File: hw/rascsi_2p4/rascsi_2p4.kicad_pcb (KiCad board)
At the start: 2 copper layers, 65 x 56 mm, 126 parts, among them J1 Raspberry_Pi_2_3, J10 Conn_01x04_Male, J2 DNP, J20 171826-4, J3 Conn_02x25_Odd_Even, J4 I2C Pinout, J5 DNP, J6 CONNFLY DB-25, J7 DNP, J8 USB_B_Micro, J9 Conn_02x25_Odd_Even, U1 74ALVC164245DGG, U2 74ALVC164245DGG, X1 Mac, X3 Mac, X7 Pi, X8 Pi

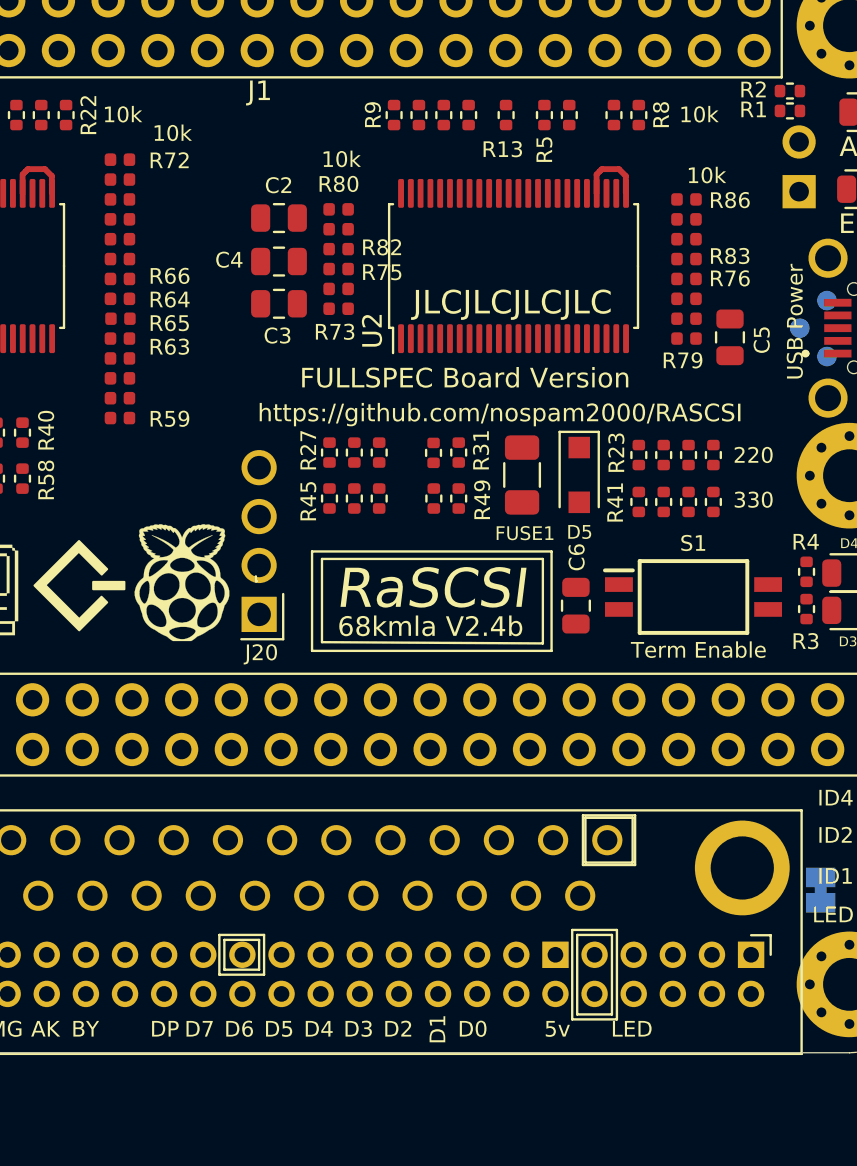
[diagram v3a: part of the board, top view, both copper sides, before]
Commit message: replaced R59-R86 by 100k to reduce power dissipation
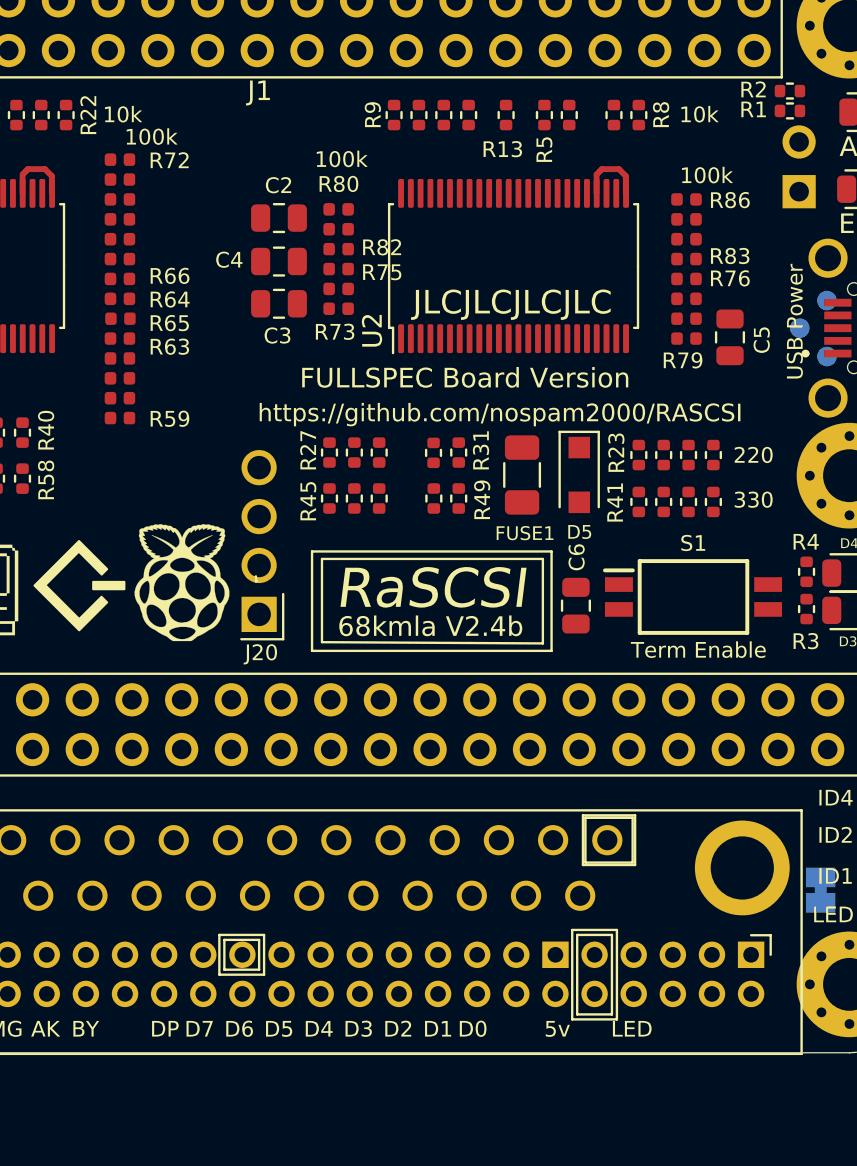
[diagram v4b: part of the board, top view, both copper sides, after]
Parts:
- R59, R60, R61, R62, R63, R64, R65, R66, R67, R68, R69, R70, R71, R72, R73, R74, R75, R76, R77, R78, R79, R80, R81, R82, R83, R84, R85, R86: value 10k -> 100k
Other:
- board text added: "100k"
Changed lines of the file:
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@@
       (effects (font (size 0.8 0.8) (thickness 0.15)))
     )
-    (fp_text value 10k (at 0 1.17) (layer F.Fab)
+    (fp_text value 100k (at 0 1.17) (layer F.Fab)
       (effects (font (size 1 1) (thickness 0.15)))
     )
@@
       (effects (font (size 1 1) (thickness 0.15)))
     )
-    (fp_text value 10k (at 0 1.17) (layer F.Fab)
+    (fp_text value 100k (at 0 1.17) (layer F.Fab)
       (effects (font (size 1 1) (thickness 0.15)))
     )
@@
       (effects (font (size 1 1) (thickness 0.15)))
     )
-    (fp_text value 10k (at 0 1.17) (layer F.Fab)
+    (fp_text value 100k (at 0 1.17) (layer F.Fab)
       (effects (font (size 1 1) (thickness 0.15)))
     )
@@
       (effects (font (size 0.8 0.8) (thickness 0.15)))
     )
-    (fp_text value 10k (at 0 1.17) (layer F.Fab)
+    (fp_text value 100k (at 0 1.17) (layer F.Fab)
       (effects (font (size 1 1) (thickness 0.15)))
     )
@@
       (effects (font (size 0.8 0.8) (thickness 0.15)))
     )
-    (fp_text value 10k (at 0 1.17) (layer F.Fab)
+    (fp_text value 100k (at 0 1.17) (layer F.Fab)
       (effects (font (size 1 1) (thickness 0.15)))
     )
@@
       (effects (font (size 1 1) (thickness 0.15)))
     )
-    (fp_text value 10k (at 0 1.17) (layer F.Fab)
+    (fp_text value 100k (at 0 1.17) (layer F.Fab)
       (effects (font (size 1 1) (thickness 0.15)))
     )
@@
       (effects (font (size 0.8 0.8) (thickness 0.15)))
     )
-    (fp_text value 10k (at 0 1.17) (layer F.Fab)
+    (fp_text value 100k (at 0 1.17) (layer F.Fab)
       (effects (font (size 1 1) (thickness 0.15)))
     )
@@
       (effects (font (size 0.8 0.8) (thickness 0.15)))
     )
-    (fp_text value 10k (at 0 1.17) (layer F.Fab)
+    (fp_text value 100k (at 0 1.17) (layer F.Fab)
       (effects (font (size 1 1) (thickness 0.15)))
     )
@@
       (effects (font (size 1 1) (thickness 0.15)))
     )
-    (fp_text value 10k (at 0 1.17) (layer F.Fab)
+    (fp_text value 100k (at 0 1.17) (layer F.Fab)
       (effects (font (size 1 1) (thickness 0.15)))
     )
@@
       (effects (font (size 1 1) (thickness 0.15)))
     )
-    (fp_text value 10k (at 0 1.17) (layer F.Fab)
+    (fp_text value 100k (at 0 1.17) (layer F.Fab)
       (effects (font (size 1 1) (thickness 0.15)))
     )
@@
       (effects (font (size 0.8 0.8) (thickness 0.15)))
     )
-    (fp_text value 10k (at 0 1.17) (layer F.Fab)
+    (fp_text value 100k (at 0 1.17) (layer F.Fab)
       (effects (font (size 1 1) (thickness 0.15)))
     )
@@
       (effects (font (size 0.8 0.8) (thickness 0.15)))
     )
-    (fp_text value 10k (at 0 1.17) (layer F.Fab)
+    (fp_text value 100k (at 0 1.17) (layer F.Fab)
       (effects (font (size 1 1) (thickness 0.15)))
     )
@@
       (effects (font (size 1 1) (thickness 0.15)))
     )
-    (fp_text value 10k (at 0 1.17) (layer F.Fab)
+    (fp_text value 100k (at 0 1.17) (layer F.Fab)
       (effects (font (size 1 1) (thickness 0.15)))
     )
@@
       (effects (font (size 0.8 0.8) (thickness 0.15)))
     )
-    (fp_text value 10k (at 0 1.17) (layer F.Fab)
+    (fp_text value 100k (at 0 1.17) (layer F.Fab)
       (effects (font (size 1 1) (thickness 0.15)))
     )
@@
       (effects (font (size 0.8 0.8) (thickness 0.15)))
     )
-    (fp_text value 10k (at 0 1.17) (layer F.Fab)
+    (fp_text value 100k (at 0 1.17) (layer F.Fab)
       (effects (font (size 1 1) (thickness 0.15)))
     )
@@
       (effects (font (size 1 1) (thickness 0.15)))
     )
-    (fp_text value 10k (at 0 1.17) (layer F.Fab)
+    (fp_text value 100k (at 0 1.17) (layer F.Fab)
       (effects (font (size 1 1) (thickness 0.15)))
     )
@@
       (effects (font (size 1 1) (thickness 0.15)))
     )
-    (fp_text value 10k (at 0 1.17) (layer F.Fab)
+    (fp_text value 100k (at 0 1.17) (layer F.Fab)
       (effects (font (size 1 1) (thickness 0.15)))
     )
@@
       (effects (font (size 1 1) (thickness 0.15)))
     )
-    (fp_text value 10k (at 0 1.17) (layer F.Fab)
+    (fp_text value 100k (at 0 1.17) (layer F.Fab)
       (effects (font (size 1 1) (thickness 0.15)))
     )
@@
       (effects (font (size 1 1) (thickness 0.15)))
     )
-    (fp_text value 10k (at 0 1.17) (layer F.Fab)
+    (fp_text value 100k (at 0 1.17) (layer F.Fab)
       (effects (font (size 1 1) (thickness 0.15)))
     )
@@
       (effects (font (size 1 1) (thickness 0.15)))
     )
-    (fp_text value 10k (at 0 1.17) (layer F.Fab)
+    (fp_text value 100k (at 0 1.17) (layer F.Fab)
       (effects (font (size 1 1) (thickness 0.15)))
     )
@@
       (effects (font (size 0.8 0.8) (thickness 0.15)))
     )
-    (fp_text value 10k (at 0 1.17) (layer F.Fab)
+    (fp_text value 100k (at 0 1.17) (layer F.Fab)
       (effects (font (size 1 1) (thickness 0.15)))
     )
@@
       (effects (font (size 0.8 0.8) (thickness 0.15)))
     )
-    (fp_text value 10k (at 0 1.17) (layer F.Fab)
+    (fp_text value 100k (at 0 1.17) (layer F.Fab)
       (effects (font (size 1 1) (thickness 0.15)))
     )
@@
       (effects (font (size 0.8 0.8) (thickness 0.15)))
     )
-    (fp_text value 10k (at 0 1.17) (layer F.Fab)
+    (fp_text value 100k (at 0 1.17) (layer F.Fab)
       (effects (font (size 1 1) (thickness 0.15)))
     )
@@
       (effects (font (size 0.8 0.8) (thickness 0.15)))
     )
-    (fp_text value 10k (at 0 1.17) (layer F.Fab)
+    (fp_text value 100k (at 0 1.17) (layer F.Fab)
       (effects (font (size 1 1) (thickness 0.15)))
     )
@@
       (effects (font (size 1 1) (thickness 0.15)))
     )
-    (fp_text value 10k (at 0 1.17) (layer F.Fab)
+    (fp_text value 100k (at 0 1.17) (layer F.Fab)
       (effects (font (size 1 1) (thickness 0.15)))
     )
@@
       (effects (font (size 1 1) (thickness 0.15)))
     )
-    (fp_text value 10k (at 0 1.17) (layer F.Fab)
+    (fp_text value 100k (at 0 1.17) (layer F.Fab)
       (effects (font (size 1 1) (thickness 0.15)))
     )
@@
       (effects (font (size 1 1) (thickness 0.15)))
     )
-    (fp_text value 10k (at 0 1.17) (layer F.Fab)
+    (fp_text value 100k (at 0 1.17) (layer F.Fab)
       (effects (font (size 1 1) (thickness 0.15)))
     )
@@
       (effects (font (size 0.8 0.8) (thickness 0.15)))
     )
-    (fp_text value 10k (at 0 1.17) (layer F.Fab)
+    (fp_text value 100k (at 0 1.17) (layer F.Fab)
       (effects (font (size 1 1) (thickness 0.15)))
     )
@@
     )
   )
-  (gr_text 10k (at 201.381 51.5145) (layer F.SilkS)
+  (gr_text 100k (at 200.3015 51.705) (layer F.SilkS)
     (effects (font (size 0.8 0.8) (thickness 0.15)))
   )
-  (gr_text 10k (at 210.017 52.848) (layer F.SilkS)
+  (gr_text 100k (at 210.017 52.848) (layer F.SilkS)
     (effects (font (size 0.8 0.8) (thickness 0.15)))
   )
-  (gr_text 10k (at 228.686 53.6735) (layer F.SilkS)
+  (gr_text 100k (at 228.686 53.6735) (layer F.SilkS)
     (effects (font (size 0.8 0.8) (thickness 0.15)))
   )
@@
     (effects (font (size 0.8 0.8) (thickness 0.15)))
   )
-  (gr_text D1 (at 214.97 97.298 90) (layer F.SilkS)
+  (gr_text D1 (at 214.97 97.298) (layer F.SilkS)
     (effects (font (size 0.8 0.8) (thickness 0.15)))
   )

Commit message: fixed some silkscreen texts removed 2nd JLC... mark fixed overlapping termpower text fixed version on backside
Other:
- board text added: "68kmla Version 2.4b"
- board text removed: "68kmla Version 2.4a"

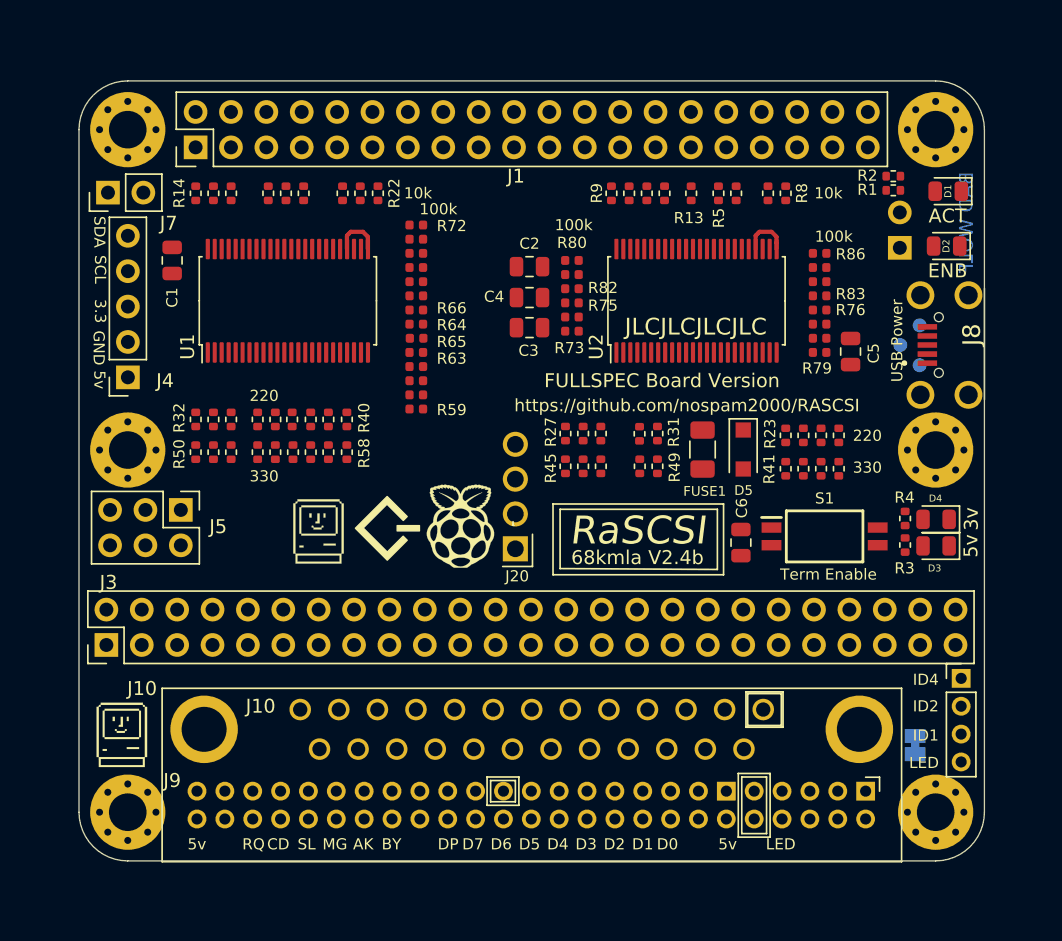
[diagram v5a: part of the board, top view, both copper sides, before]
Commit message: imported spectra routing data with 111 vias
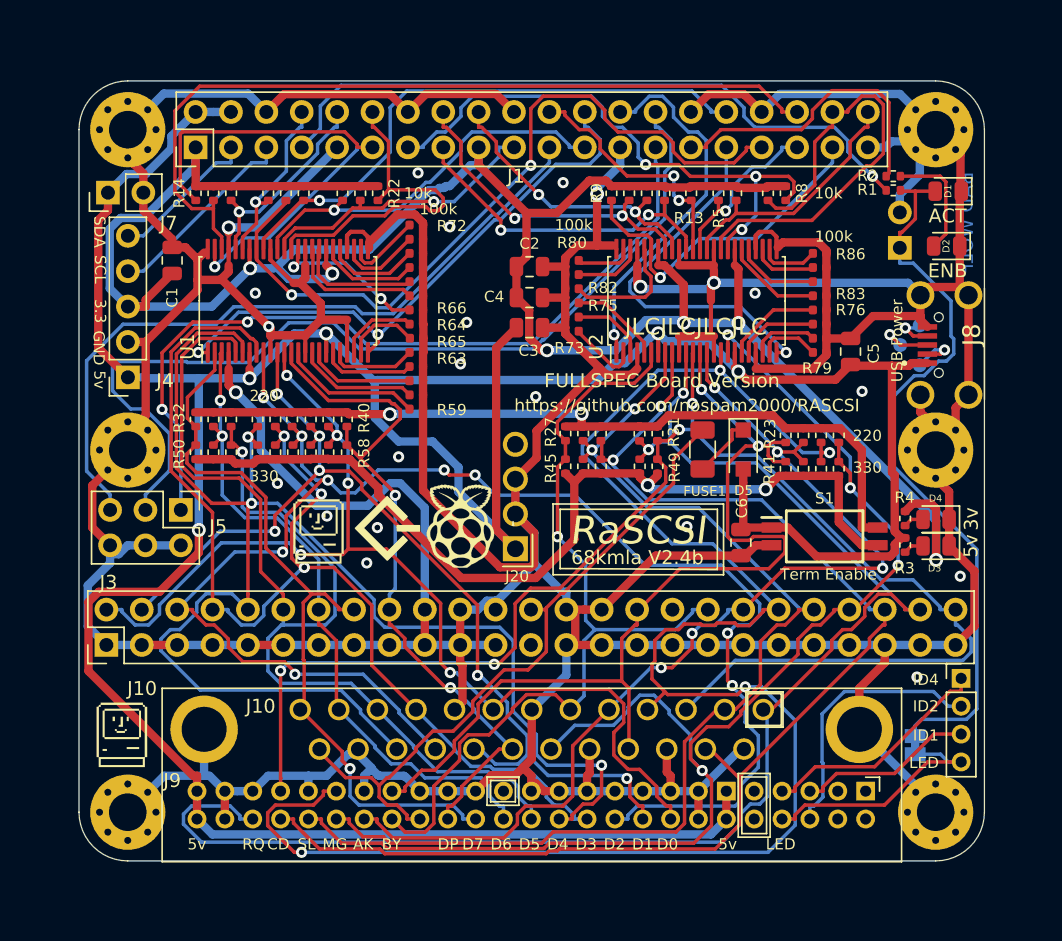
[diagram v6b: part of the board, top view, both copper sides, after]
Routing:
- net GND: track 7.16 -> 640.0 mm, vias 0 -> 23
- net +5V: track 0.00 -> 242.7 mm, vias 0 -> 5
- net +3V3: track 0.00 -> 167.3 mm, vias 0 -> 6
- net C-RST: track 0.00 -> 125.4 mm, vias 0 -> 4
- net C-D2: track 0.00 -> 115.7 mm, vias 0 -> 9
- net C-D4: track 0.00 -> 108.2 mm, vias 0 -> 3
- net C-REQ: track 0.00 -> 106.6 mm, vias 0 -> 2
- net C-I_O: track 0.00 -> 105.6 mm, vias 0 -> 4
- net C-SEL: track 0.00 -> 100.7 mm, vias 0 -> 4
- net C-C_D: track 0.00 -> 94.1 mm, vias 0 -> 2
- net C-D3: track 0.00 -> 81.7 mm, vias 0 -> 3
- net C-D5: track 0.00 -> 79.8 mm, vias 0 -> 1
- net C-MSG: track 0.00 -> 79.4 mm, vias 0 -> 2
- net C-D0: track 0.00 -> 78.1 mm, vias 0 -> 5
- net C-ACK: track 0.00 -> 73.1 mm, vias 0 -> 5
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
